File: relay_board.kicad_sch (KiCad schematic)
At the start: 12 parts, among them J3 J_PRECURSOR_A, J6 J_FORELINE_VALVE, J7 J_N2_PURGE, J8 J_SPARE, K1 Relay 2, K2 Relay 1, K3 Relay 3, K4 Relay 4

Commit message: Clean up duplicates in schematic components
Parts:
- renumbered J6 to J5, J3 to J6
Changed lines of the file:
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@@
 		(on_board yes)
 		(dnp no)
-		(property "Reference" "J6"
+		(property "Reference" "J5"
 			(at 63.5 74.9299 0)
 			(effects
@@
 				)
 				(justify left)
-				(hide yes)
 			)
 		)
@@
 			(project "ald_control_board"
 				(path "/0db39e9c-e7a7-46b4-b6c2-b1f3e7389c4f/f7c6a359-8623-4d62-a80b-5dc912748245"
-					(reference "J6")
+					(reference "J5")
 					(unit 1)
 				)
@@
 				)
 				(justify left)
-				(hide yes)
 			)
 		)
@@
 		(on_board yes)
 		(dnp no)
-		(property "Reference" "J3"
+		(property "Reference" "J6"
 			(at 128.27 73.6599 0)
 			(effects
@@
 				)
 				(justify left)
-				(hide yes)
 			)
 		)
@@
 			(project ""
 				(path "/0db39e9c-e7a7-46b4-b6c2-b1f3e7389c4f/f7c6a359-8623-4d62-a80b-5dc912748245"
-					(reference "J3")
+					(reference "J6")
 					(unit 1)
 				)
@@
 				)
 				(justify left)
-				(hide yes)
-			)
-		)
+			)
+		)

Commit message: Clean up duplicates in schematic components and assign footprints
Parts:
- D1, D2, D3, D4: footprint (none) -> Diode_THT:D_DO-41_SOD81_P10.16mm_Horizontal
- J5, J6, J7, J8: footprint (none) -> TerminalBlock_Phoenix:TerminalBlock_Phoenix_MKDS-1,5-2-5.08_1x02_P5.08mm_Horizontal
- K1, K2, K3, K4: footprint (none) -> Relay_THT:Relay_SPST_SANYOU_SRD_Series_Form_A
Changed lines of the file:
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@@
 			)
 		)
-		(property "Footprint" ""
+		(property "Footprint" "Diode_THT:D_DO-41_SOD81_P10.16mm_Horizontal"
 			(at 158.75 85.09 0)
 			(effects
@@
 			)
 		)
-		(property "Footprint" ""
+		(property "Footprint" "Diode_THT:D_DO-41_SOD81_P10.16mm_Horizontal"
 			(at 226.06 85.09 0)
 			(effects
@@
 			)
 		)
-		(property "Footprint" ""
+		(property "Footprint" "TerminalBlock_Phoenix:TerminalBlock_Phoenix_MKDS-1,5-2-5.08_1x02_P5.08mm_Horizontal"
 			(at 60.96 74.93 0)
 			(effects
@@
 			)
 		)
-		(property "Footprint" ""
+		(property "Footprint" "TerminalBlock_Phoenix:TerminalBlock_Phoenix_MKDS-1,5-2-5.08_1x02_P5.08mm_Horizontal"
 			(at 260.35 73.66 0)
 			(effects
@@
 			)
 		)
-		(property "Footprint" ""
+		(property "Footprint" "Relay_THT:Relay_SPST_SANYOU_SRD_Series_Form_A"
 			(at 186.69 86.36 0)
 			(effects
@@
 			)
 		)
-		(property "Footprint" ""
+		(property "Footprint" "Diode_THT:D_DO-41_SOD81_P10.16mm_Horizontal"
 			(at 91.44 85.09 0)
 			(effects
@@
 			)
 		)
-		(property "Footprint" ""
+		(property "Footprint" "TerminalBlock_Phoenix:TerminalBlock_Phoenix_MKDS-1,5-2-5.08_1x02_P5.08mm_Horizontal"
 			(at 125.73 73.66 0)
 			(effects
@@
 			)
 		)
-		(property "Footprint" ""
+		(property "Footprint" "Diode_THT:D_DO-41_SOD81_P10.16mm_Horizontal"
 			(at 26.67 86.36 0)
 			(effects
@@
 			)
 		)
-		(property "Footprint" ""
+		(property "Footprint" "Relay_THT:Relay_SPST_SANYOU_SRD_Series_Form_A"
 			(at 119.38 86.36 0)
 			(effects
@@
 			)
 		)
-		(property "Footprint" ""
+		(property "Footprint" "TerminalBlock_Phoenix:TerminalBlock_Phoenix_MKDS-1,5-2-5.08_1x02_P5.08mm_Horizontal"
 			(at 193.04 73.66 0)
 			(effects
@@
 			)
 		)
-		(property "Footprint" ""
+		(property "Footprint" "Relay_THT:Relay_SPST_SANYOU_SRD_Series_Form_A"
 			(at 54.61 87.63 0)
 			(effects
@@
 			)
 		)
-		(property "Footprint" ""
+		(property "Footprint" "Relay_THT:Relay_SPST_SANYOU_SRD_Series_Form_A"
 			(at 254 86.36 0)
 			(effects

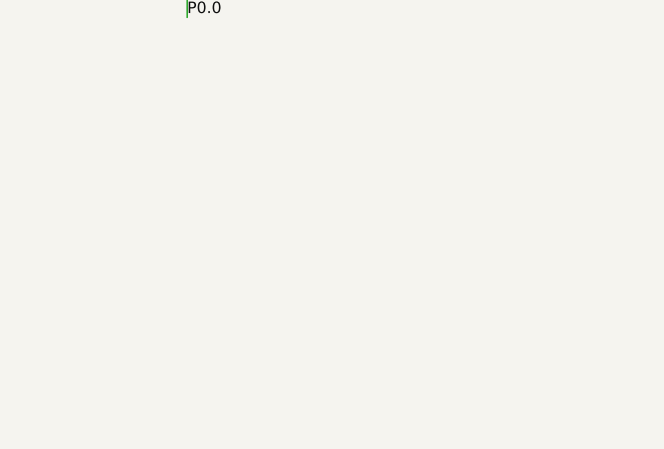
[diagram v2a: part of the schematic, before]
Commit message: 5 relays
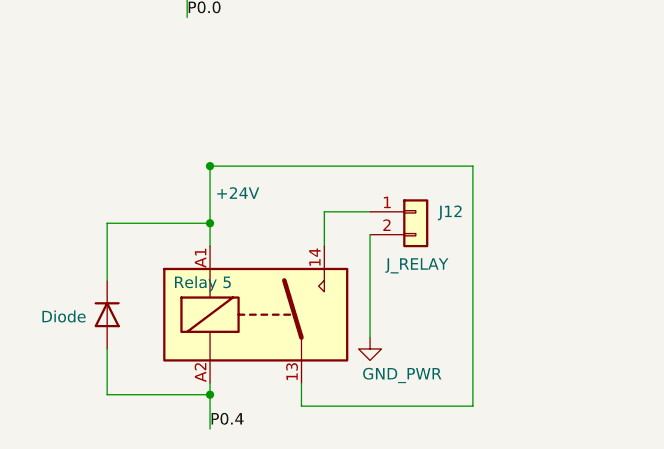
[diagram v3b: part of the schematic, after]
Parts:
- added D5: Diode, Diode_THT:D_DO-41_SOD81_P10.16mm_Horizontal, symbol Device:D
- added J12: J_RELAY, TerminalBlock_Phoenix:TerminalBlock_Phoenix_MKDS-1,5-2-5.08_1x02_P5.08mm_Horizontal, symbol Connector_Generic:Conn_01x02
- added K5: Relay 5, Relay_THT:Relay_SPST_SANYOU_SRD_Series_Form_A, symbol Relay:Relay_SPST-NO
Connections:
- net +24V: now also D5.1 (K), K5.13, K5.A1
- net GND_PWR: now also J12.2 (Pin_2)
- new net: J12.1 (Pin_1), K5.14
- new net P0.4: D5.2 (A), K5.A2
